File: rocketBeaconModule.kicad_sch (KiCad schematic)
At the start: 42 parts, among them J1 TYPE-C-31-M-12, J2 PWR, J3 GND, J4 PWR, J5 GND, U1 STM32F401CCU6, U2 CP2102N-Axx-xQFN20, Y1 16MHz

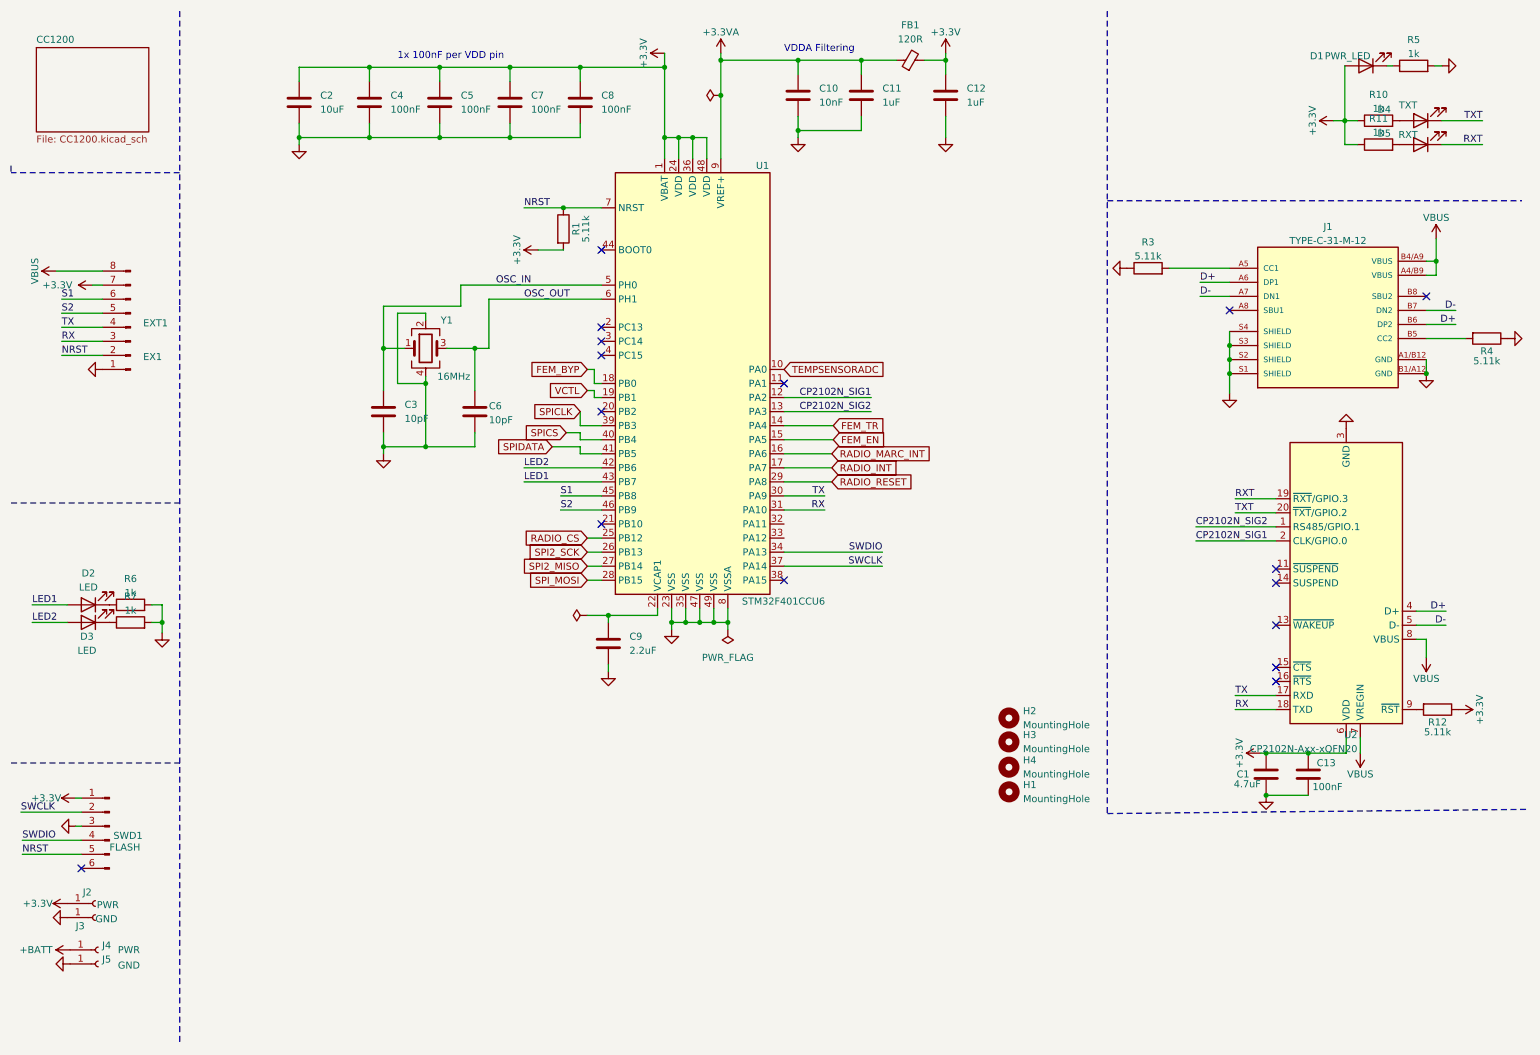
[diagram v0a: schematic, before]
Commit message: reference/backup for mostly routed pcb
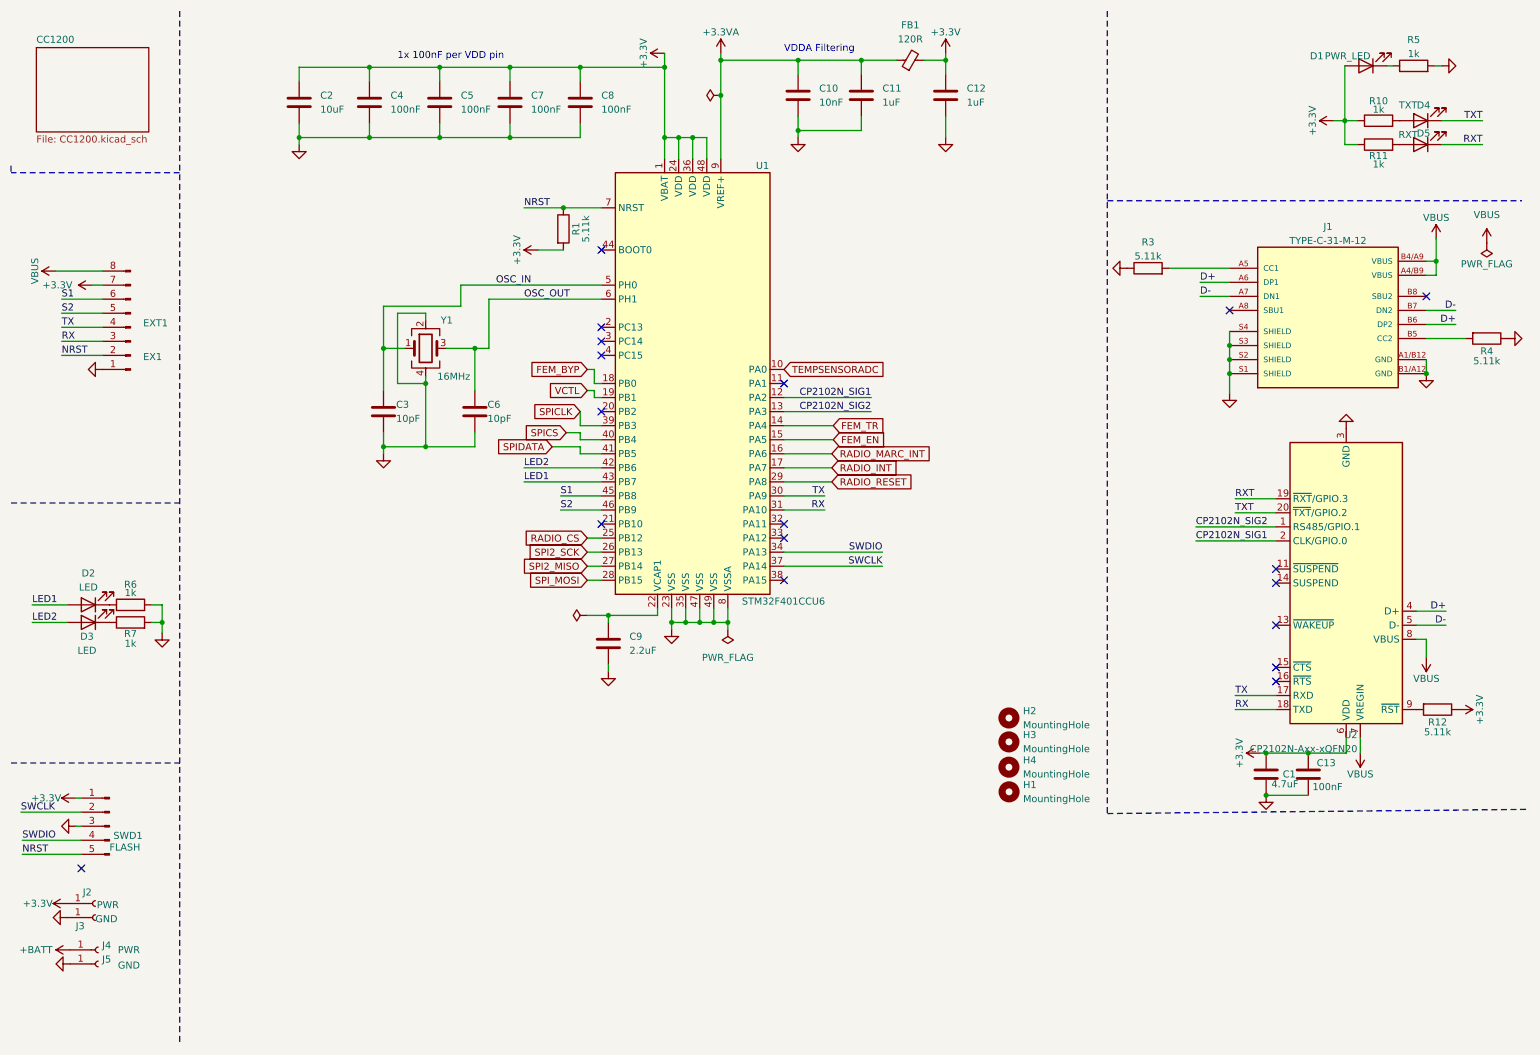
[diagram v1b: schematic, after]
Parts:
- C1: footprint Capacitor_SMD:C_0603_1608Metric -> Capacitor_SMD:C_0402_1005Metric; LCSC (none) -> C23733; LCSC Part C71631 -> (none)
- C10: LCSC (none) -> C15195; LCSC Part C15195 -> (none)
- C11, C12: LCSC (none) -> C52923; LCSC Part C52923 -> (none)
- C13: LCSC (none) -> C307331; LCSC Part C307331 -> (none)
- C2: footprint Capacitor_SMD:C_0603_1608Metric -> Capacitor_SMD:C_0402_1005Metric; LCSC (none) -> C7472949; LCSC Part c -> (none)
- C3, C6: LCSC (none) -> C32949; LCSC Part C32949 -> (none)
- C4, C5, C7, C8: LCSC (none) -> C1525; LCSC Part C307331 -> (none)
- C9: LCSC (none) -> C12530; LCSC Part C12530 -> (none)
- D1: LCSC (none) -> C130722; LCSC Part C5160717 -> (none)
- D2: LCSC (none) -> C131223; LCSC Part C131223 -> (none)
- D3, D5: LCSC (none) -> C130722; LCSC Part C130722 -> (none)
- D4: LCSC (none) -> C136765; LCSC Part C136765 -> (none)
- EX1: LCSC (none) -> C132510; LCSC Part C132510 -> (none)
- FB1: LCSC (none) -> C85831; LCSC Part C85831 -> (none)
- R1, R12, R3, R4: LCSC (none) -> C274895; LCSC Part C25906 -> (none)
- R10, R5, R6, R7: LCSC (none) -> C11702; LCSC Part C11702 -> (none)
- SWD1: symbol Connector:Conn_01x06_Male -> Connector:Conn_01x05_Pin
- Y1: LCSC (none) -> C13738; LCSC Part C13738 -> (none)
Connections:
- no-connect marks 16 -> 18

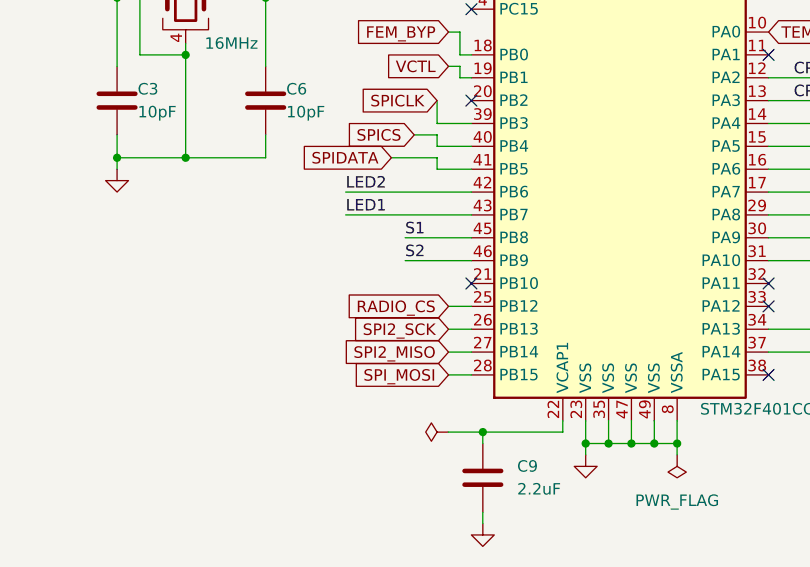
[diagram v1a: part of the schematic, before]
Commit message: finished routing pcb and passed DRC, waiting for review by Ethan
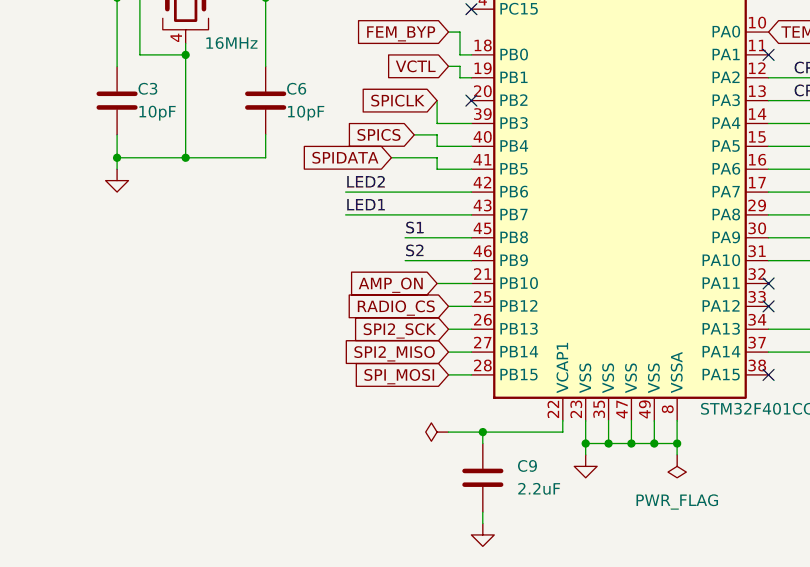
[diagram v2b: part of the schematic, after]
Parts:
- U2: LCSC (none) -> C969913; LCSC Part C969913 -> (none)
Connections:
- net AMP_ON: now reaches U1.21 (PB10)
- no-connect marks 18 -> 17
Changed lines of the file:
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@@
 	)
 	(no_connect
-		(at 118.11 104.14)
-	)
-	(no_connect
 		(at 118.11 68.58)
 	)
@@
 	(wire
 		(pts
+			(xy 114.3 104.14) (xy 118.11 104.14)
+		)
+		(stroke
+			(width 0)
+			(type default)
+		)
+	)
+	(wire
+		(pts
 			(xy 116.84 76.2) (xy 116.84 78.74)
 		)
@@
 		)
 	)
+	(global_label "AMP_ON"
+		(shape input)
+		(at 114.3 104.14 180)
+		(fields_autoplaced yes)
+		(effects
+			(font
+				(size 1.27 1.27)
+			)
+			(justify right)
+		)
+		(property "Intersheetrefs" "${INTERSHEET_REFS}"
+			(at 103.8762 104.14 0)
+			(effects
+				(font
+					(size 1.27 1.27)
+				)
+				(justify right)
+				(hide yes)
+			)
+		)
+	)
 	(global_label "FEM_BYP"
 		(shape input)
@@
 			)
 		)
-		(property "LCSC Part" "C969913"
+		(property "LCSC" "C969913"
 			(at 252.73 114.808 0)
 			(effects

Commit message: Revert "Stephen"
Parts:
- C1: footprint Capacitor_SMD:C_0402_1005Metric -> Capacitor_SMD:C_0603_1608Metric; LCSC C23733 -> (none); LCSC Part (none) -> C71631
- C10: LCSC C15195 -> (none); LCSC Part (none) -> C15195
- C11, C12: LCSC C52923 -> (none); LCSC Part (none) -> C52923
- C13: LCSC C307331 -> (none); LCSC Part (none) -> C307331
- C2: footprint Capacitor_SMD:C_0402_1005Metric -> Capacitor_SMD:C_0603_1608Metric; LCSC C7472949 -> (none); LCSC Part (none) -> c
- C3, C6: LCSC C32949 -> (none); LCSC Part (none) -> C32949
- C4, C5, C7, C8: LCSC C1525 -> (none); LCSC Part (none) -> C307331
- C9: LCSC C12530 -> (none); LCSC Part (none) -> C12530
- D1: LCSC C130722 -> (none); LCSC Part (none) -> C5160717
- D2: LCSC C131223 -> (none); LCSC Part (none) -> C131223
- D3, D5: LCSC C130722 -> (none); LCSC Part (none) -> C130722
- D4: LCSC C136765 -> (none); LCSC Part (none) -> C136765
- EX1: LCSC C132510 -> (none); LCSC Part (none) -> C132510
- FB1: LCSC C85831 -> (none); LCSC Part (none) -> C85831
- R1, R12, R3, R4: LCSC C274895 -> (none); LCSC Part (none) -> C25906
- R10, R5, R6, R7: LCSC C11702 -> (none); LCSC Part (none) -> C11702
- SWD1: symbol Connector:Conn_01x05_Pin -> Connector:Conn_01x06_Male
- U2: LCSC C969913 -> (none); LCSC Part (none) -> C969913
- Y1: LCSC C13738 -> (none); LCSC Part (none) -> C13738
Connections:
- net AMP_ON: no longer names the net of U1.21 (PB10)
- net SPICLK: no longer names the net of U1.39 (PB3)
- net SPICS: no longer names the net of U1.40 (PB4)
- net SPIDATA: no longer names the net of U1.41 (PB5)
- net TEMPSENSORADC: no longer names the net of U1.10 (PA0)
- net VCTL: no longer names the net of U1.19 (PB1)
- no-connect marks 17 -> 21
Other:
- moved on the sheet: C3, Y1

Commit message: completed most of radio schematic
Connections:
- net VCTL1: now reaches U1.19 (PB1)
- net VCTL2: now reaches U1.20 (PB2)
- no-connect marks 21 -> 19
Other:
- moved on the sheet: C3, C6, Y1

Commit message: changed rf switch, updated rf amp footprint and updated schematic
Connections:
- net THERMISTORADC: now reaches U1.10 (PA0)
- net VCTL1 renamed VCTL
- net VCTL2: no longer names the net of U1.20 (PB2)
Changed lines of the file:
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@@
 	)
 	(no_connect
-		(at 151.13 76.2)
+		(at 267.208 62.992)
 	)
 	(no_connect
-		(at 267.208 62.992)
+		(at 118.11 83.82)
 	)
 	(no_connect
@@
 	(wire
 		(pts
-			(xy 118.11 83.82) (xy 116.84 83.82)
-		)
-		(stroke
-			(width 0)
-			(type default)
-		)
-	)
-	(wire
-		(pts
 			(xy 220.726 57.912) (xy 231.648 57.912)
 		)
@@
 	(wire
 		(pts
-			(xy 137.16 140.97) (xy 144.78 140.97)
-		)
-		(stroke
-			(width 0)
-			(type default)
-		)
-	)
-	(wire
-		(pts
 			(xy 88.9 34.29) (xy 76.2 34.29)
 		)
@@
 	(wire
 		(pts
-			(xy 147.32 140.97) (xy 152.4 140.97)
-		)
-		(stroke
-			(width 0)
-			(type default)
-		)
-	)
-	(wire
-		(pts
-			(xy 116.84 85.09) (xy 115.57 85.09)
-		)
-		(stroke
-			(width 0)
-			(type default)
-		)
-	)
-	(wire
-		(pts
 			(xy 86.36 78.74) (xy 86.36 90.17)
 		)
@@
 	(wire
 		(pts
-			(xy 116.84 83.82) (xy 116.84 85.09)
-		)
-		(stroke
-			(width 0)
-			(type default)
-		)
-	)
-	(wire
-		(pts
 			(xy 95.25 87.63) (xy 95.25 90.17)
 		)
@@
 		)
 	)
-	(label "FVPC"
-		(at 147.32 140.97 0)
-		(fields_autoplaced yes)
-		(effects
-			(font
-				(size 1.27 1.27)
-			)
-			(justify left bottom)
-		)
-	)
 	(label "NRST"
 		(at 20.574 73.66 0)
@@
 		)
 	)
-	(label "FVPC"
-		(at 144.78 140.97 180)
-		(fields_autoplaced yes)
-		(effects
-			(font
-				(size 1.27 1.27)
-			)
-			(justify right bottom)
-		)
-	)
 	(label "RX"
 		(at 158.496 101.6 180)
@@
 		)
 	)
-	(global_label "VCTL1"
+	(global_label "VCTL"
 		(shape input)
 		(at 115.57 81.28 180)
@@
 		)
 		(property "Intersheetrefs" "${INTERSHEET_REFS}"
-			(at 107.021 81.28 0)
+			(at 108.2305 81.28 0)
 			(effects
 				(font
@@
 		)
 	)
-	(global_label "VCTL2"
-		(shape input)
-		(at 115.57 85.09 180)
-		(fields_autoplaced yes)
-		(effects
-			(font
-				(size 1.27 1.27)
-			)
-			(justify right)
-		)
-		(property "Intersheetrefs" "${INTERSHEET_REFS}"
-			(at 107.021 85.09 0)
-			(effects
-				(font
-					(size 1.27 1.27)
-				)
-				(justify right)
-				(hide yes)
-			)
-		)
-	)
 	(global_label "RADIO_INT"
 		(shape input)
@@
 		)
 	)
-	(global_label "FEM_VPC"
+	(global_label "THERMISTORADC"
 		(shape input)
-		(at 152.4 140.97 0)
+		(at 151.13 76.2 0)
 		(fields_autoplaced yes)
 		(effects
@@
 		)
 		(property "Intersheetrefs" "${INTERSHEET_REFS}"
-			(at 163.6704 140.97 0)
+			(at 169.2947 76.2 0)
 			(effects
 				(font
@@
 					(unit 1)
 				)
-			)
-		)
-	)
-	(symbol
-		(lib_id "power:+3.3V")
-		(at 137.16 140.97 90)
-		(unit 1)
-		(exclude_from_sim no)
-		(in_bom yes)
-		(on_board yes)
-		(dnp no)
-		(property "Reference" "#PWR059"
-			(at 140.97 140.97 0)
-			(effects
-				(font
-					(size 1.27 1.27)
-				)
-				(hide yes)
-			)
-		)
-		(property "Value" "+3.3V"
-			(at 133.35 140.97 0)
-			(effects
-				(font
-					(size 1.27 1.27)
-				)
-			)
-		)
-		(property "Footprint" ""
-			(at 137.16 140.97 0)
-			(effects
-				(font
-					(size 1.27 1.27)
-				)
-				(hide yes)
-			)
-		)
-		(property "Datasheet" ""
-			(at 137.16 140.97 0)
-			(effects
-				(font
-					(size 1.27 1.27)
-				)
-				(hide yes)
-			)
-		)
-		(property "Description" ""
-			(at 137.16 140.97 0)
-			(effects
-				(font
-					(size 1.27 1.27)
-				)
-				(hide yes)
-			)
-		)
-		(pin "1"
-		)
-		(instances
-			(project "rocketBeaconModule"
-				(path "/4108571e-8c4c-4eba-a51f-04b21c4cec35"
-					(reference "#PWR059")
-					(unit 1)
-				)
